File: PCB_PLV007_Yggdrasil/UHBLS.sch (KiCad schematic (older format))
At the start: 34 parts, among them U4 74HC21

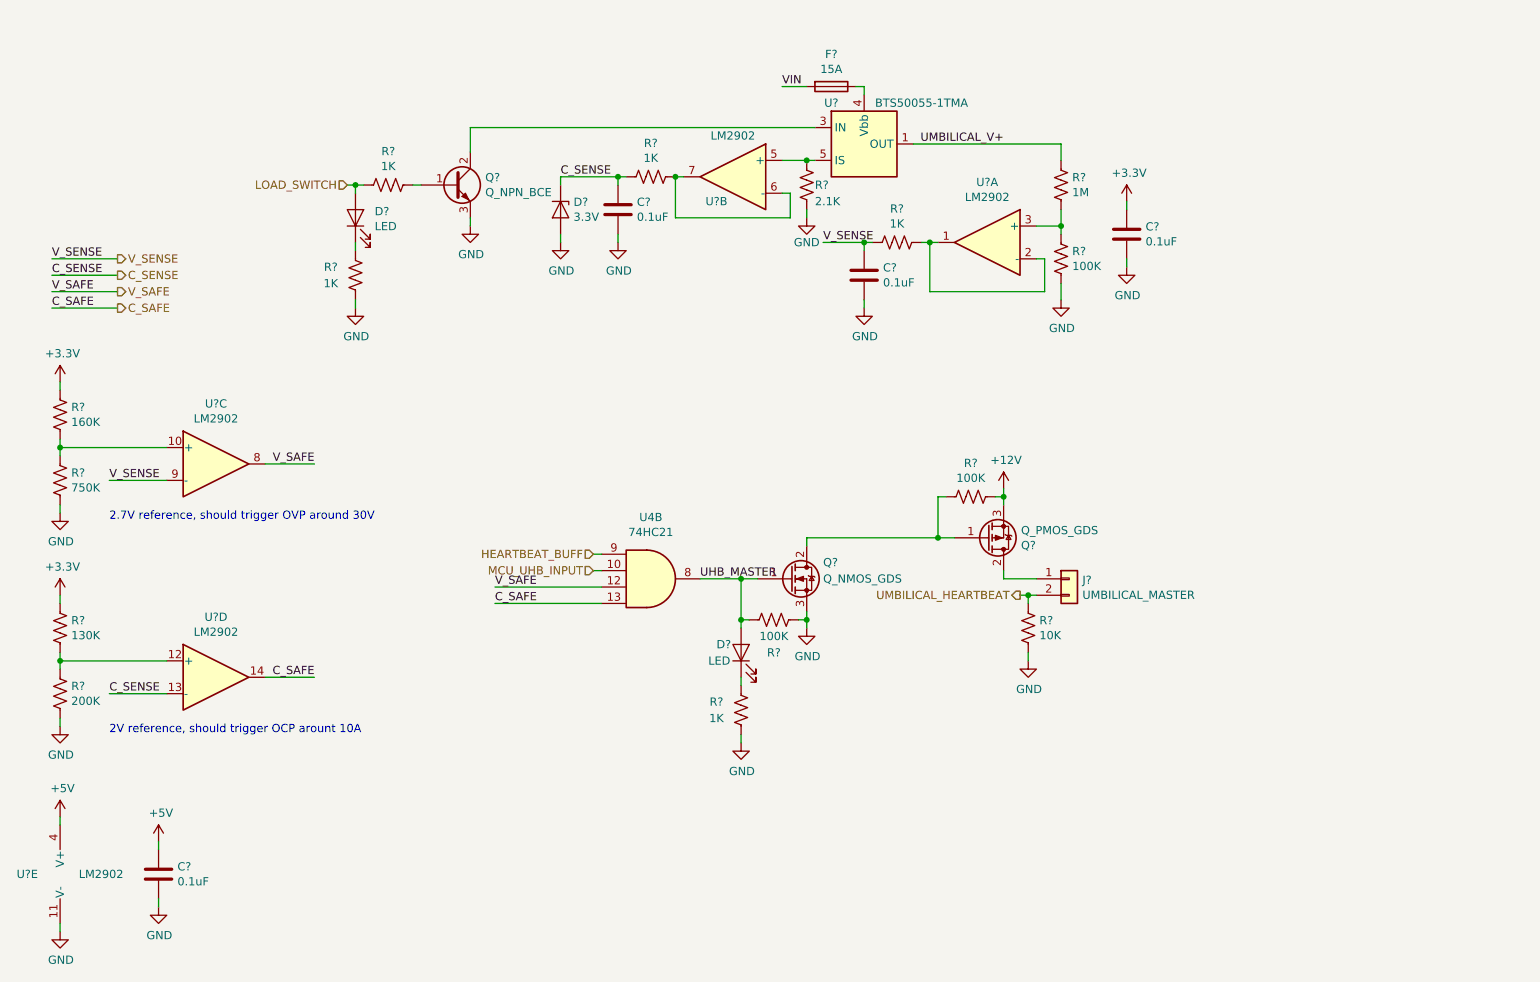
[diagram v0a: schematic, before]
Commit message: Make Yggdrasil pass ERC
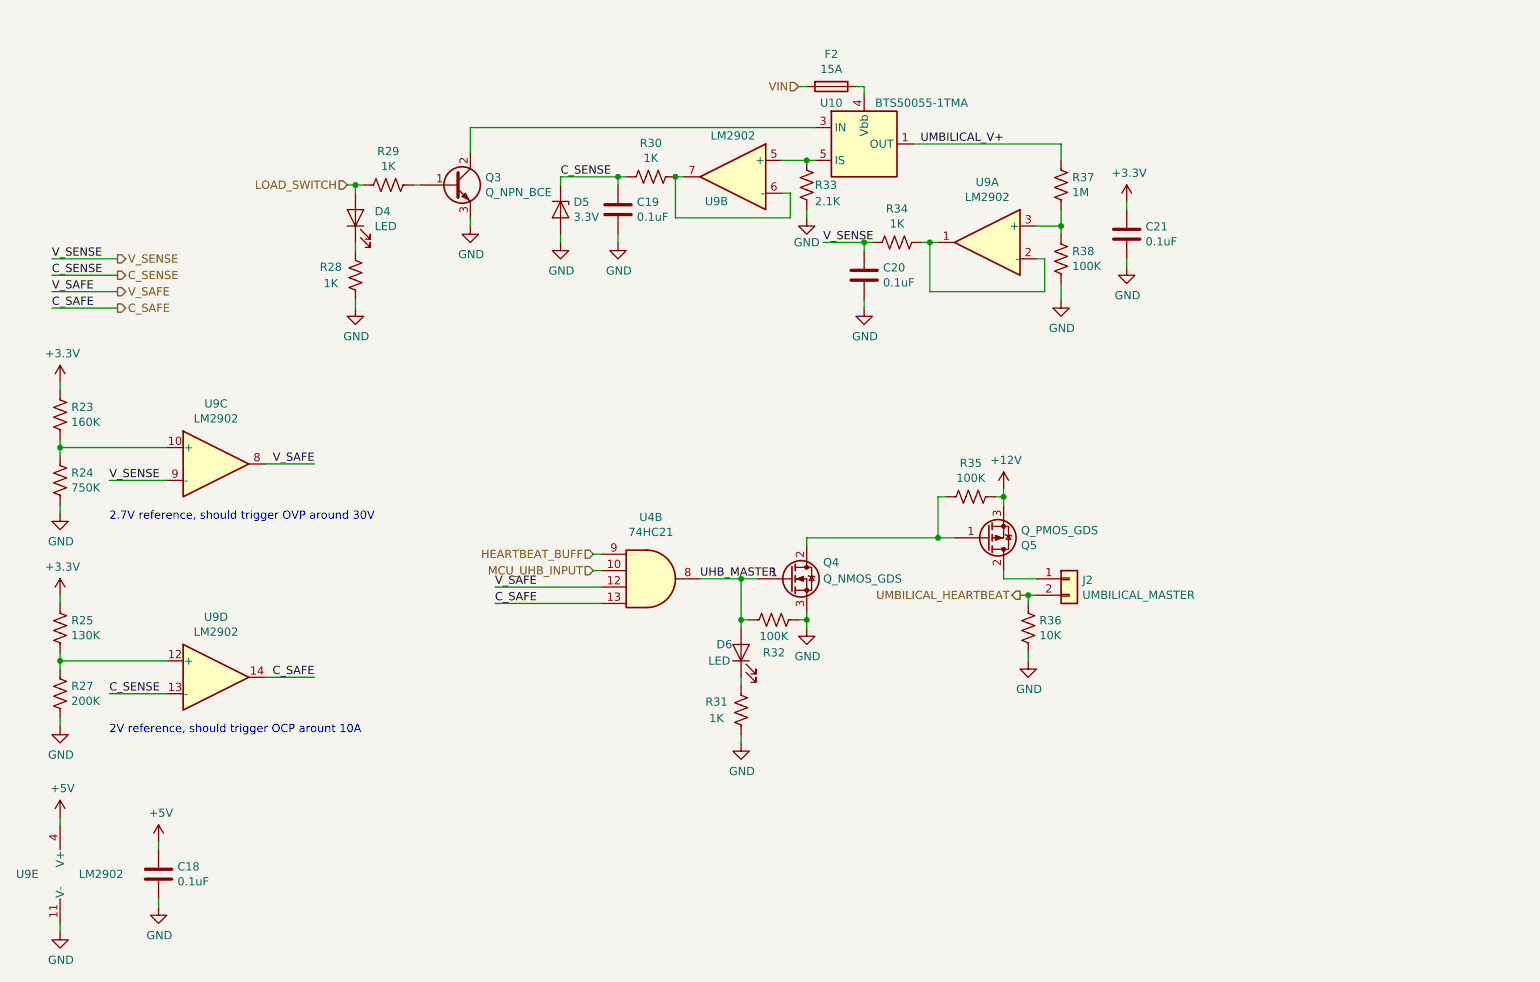
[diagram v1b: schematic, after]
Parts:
- gave numbers to parts that had none: 29

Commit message: Most of sensors for heimdal complete, still need to sort out load cells, flammable gas
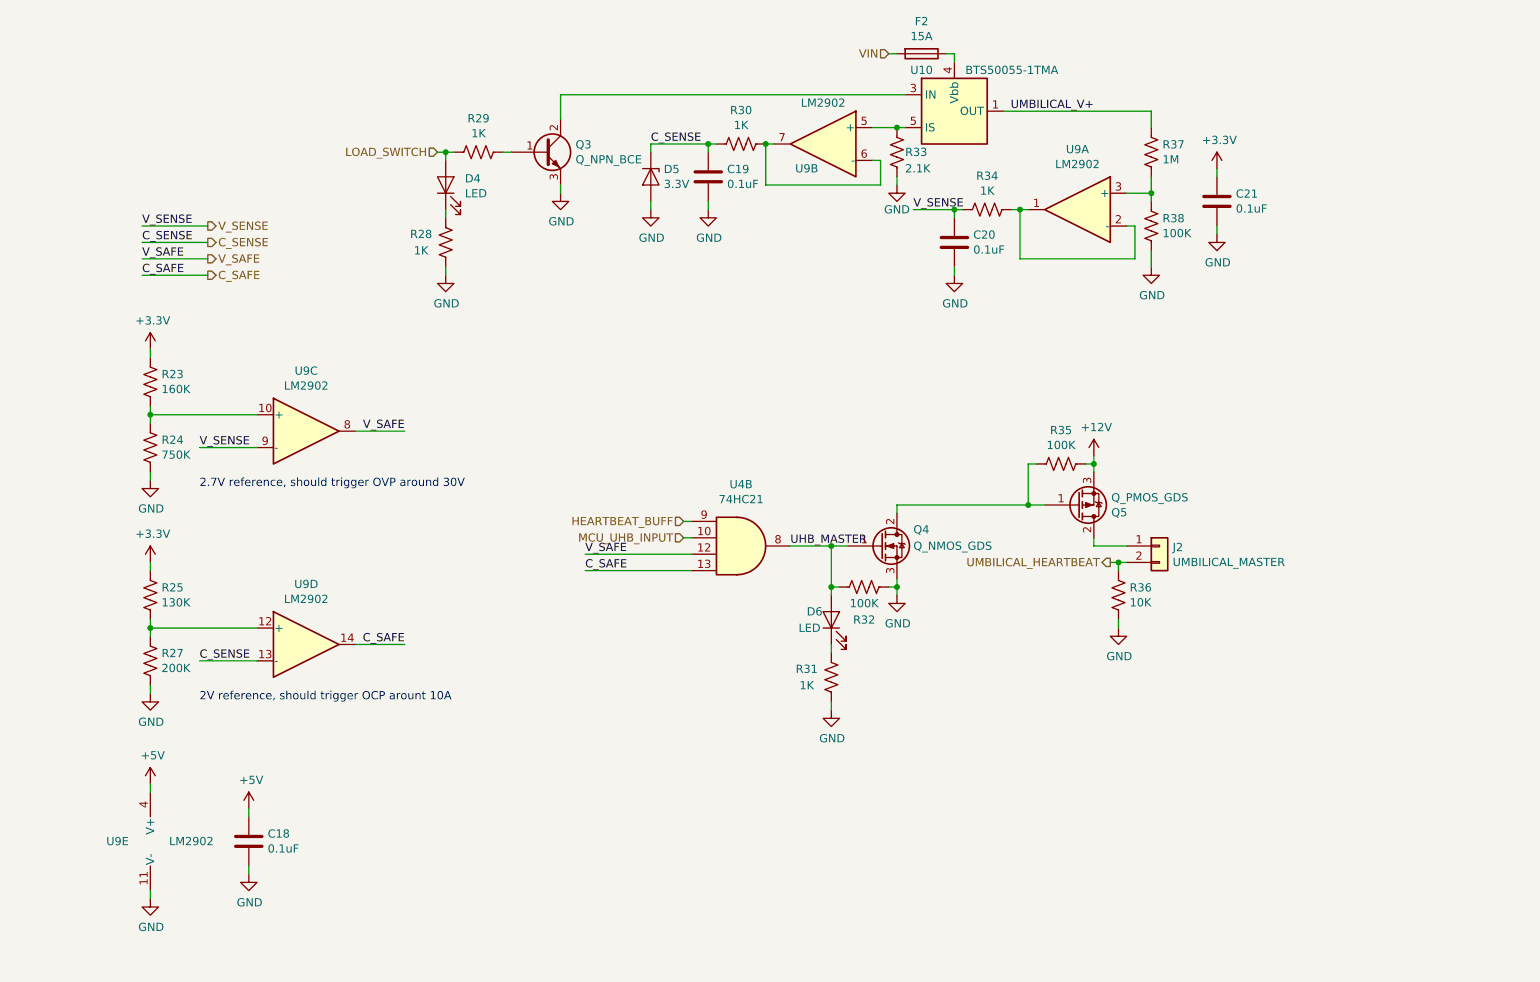
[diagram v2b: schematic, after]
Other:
- moved on the sheet: C18, C19, C20, C21, D4, D5, D6, F2, J2, Q3, Q4, Q5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

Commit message: Updates to Yggdrasil as per review by Fronk
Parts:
- added D7: 3.3V, symbol Device:D_Zener
- added J3: UMBILICAL_POWER, symbol Connector_Generic:Conn_01x04
- added R?: 260K, symbol Device:R_US
- added R?: 95K, symbol Device:R_US
- R23: value 160K -> 10K
- R24: value 750K -> 43K
- R25: value 130K -> 10K
- R27: value 200K -> 16K
- R37: value 1M -> 100K
- R38: value 100K -> 10K
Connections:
- net C_SAFE: now also R?.1
- net GND: now also D7.2 (A), J3.1 (Pin_1), J3.2 (Pin_2)
- net UMBILICAL_V+: now also J3.3 (Pin_3), J3.4 (Pin_4)
- net V_SAFE: now also R?.1
- net V_SENSE: now also D7.1 (K)
- net at R23.2, R24.1, U9.10 (+): now also R?.2
- net at R25.2, R27.1, U9.12 (+): now also R?.2
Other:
- note added: "NOTE: Place these decoupling passives\nas close as possible to signal destination."
- note added: "Should trigger OCP arount 10A\nHysteresis from 1.9V to 2.1V"
- note added: "Should trigger OVP around 30V\nHysteresis from 2.6V to 2.7V"
- note removed: "2.7V reference, should trigger OVP around 30V"
- note removed: "2V reference, should trigger OCP arount 10A"

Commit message: Add power LEDs and large input caps to Yggdrasil, Odin
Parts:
- C19, C20: value 0.1uF -> 0.47uF
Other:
- note added: "The instrumentation section here has had its functionality verified through simualtion"
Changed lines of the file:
@@
 AR Path="/5FC40E29/5FC5819D" Ref="C20"  Part="1"
 F 0 "C20" H 7065 2796 50  0000 L CNN
-F 1 "0.1uF" H 7065 2705 50  0000 L CNN
+F 1 "0.47uF" H 7065 2705 50  0000 L CNN
 F 2 "" H 6988 2600 50  0001 C CNN
 F 3 "~" H 6950 2750 50  0001 C CNN
@@
 AR Path="/5FC40E29/5FC581C0" Ref="C19"  Part="1"
 F 0 "C19" H 5565 2396 50  0000 L CNN
-F 1 "0.1uF" H 5565 2305 50  0000 L CNN
+F 1 "0.47uF" H 5565 2305 50  0000 L CNN
 F 2 "" H 5488 2200 50  0001 C CNN
 F 3 "~" H 5450 2350 50  0001 C CNN
@@
 Wire Wire Line
 	3400 5200 3700 5200
+Text Notes 6350 6550 0    50   ~ 0
+The instrumentation section here has had its functionality verified through simualtion
 $EndSCHEMATC
